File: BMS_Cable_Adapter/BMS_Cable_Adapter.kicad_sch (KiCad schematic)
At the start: 3 parts, among them J1 MicroFit_18Pin_Receptacle_Hea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, J2 MicroFit_10Pin_Receptacle_Hea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, J3 32Pin JAE

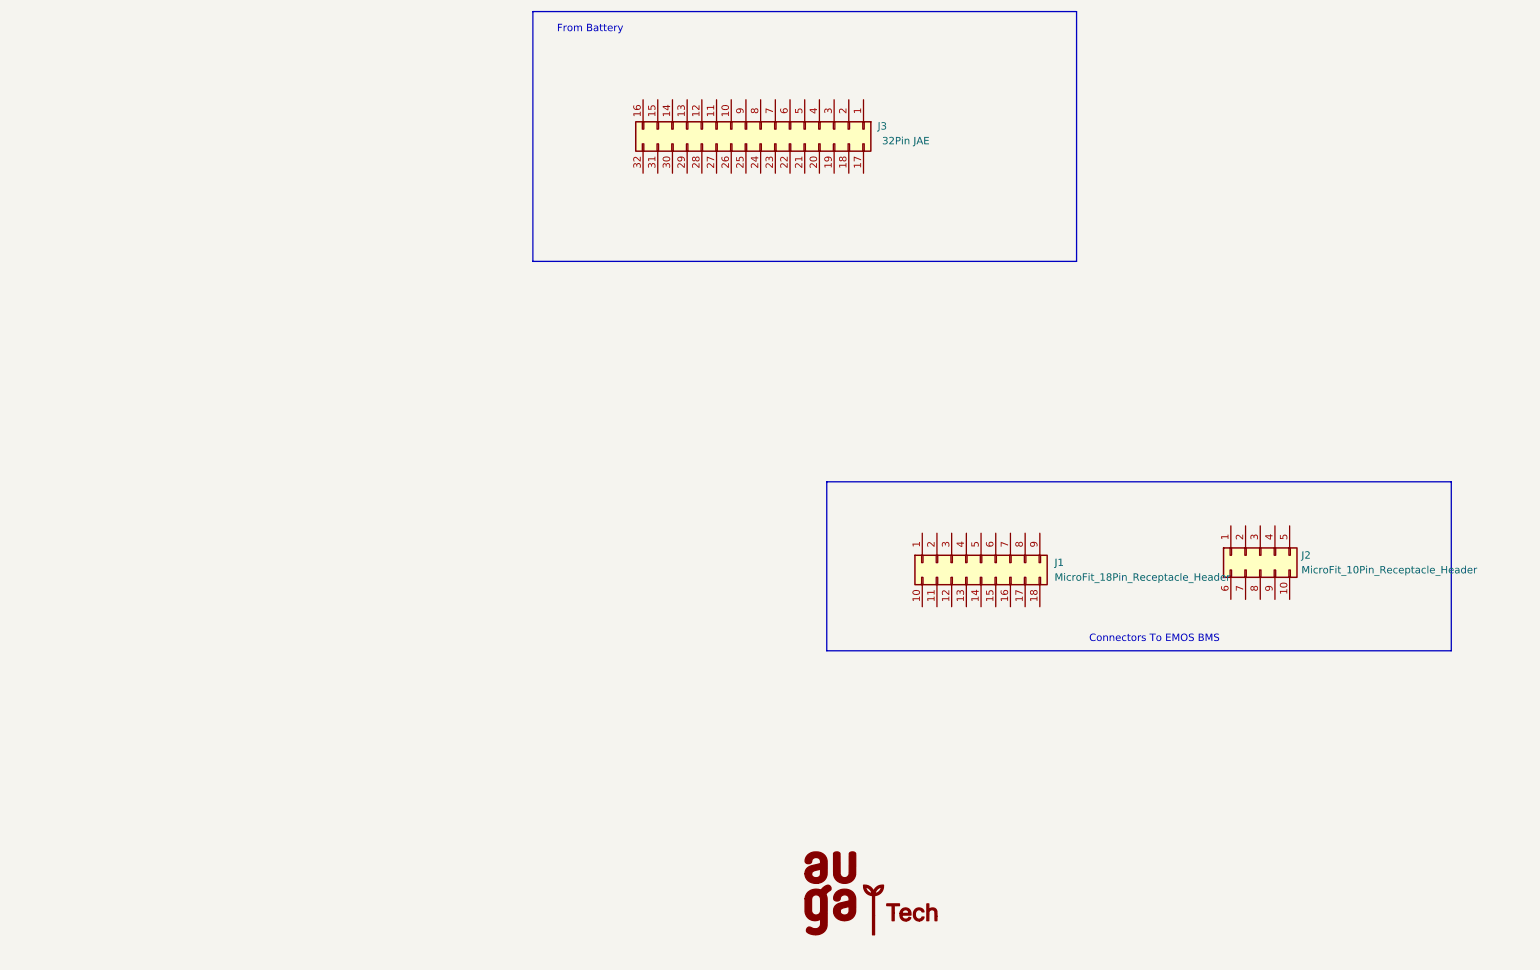
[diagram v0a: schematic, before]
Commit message: BMS Cable adapter done
Also libraries updated
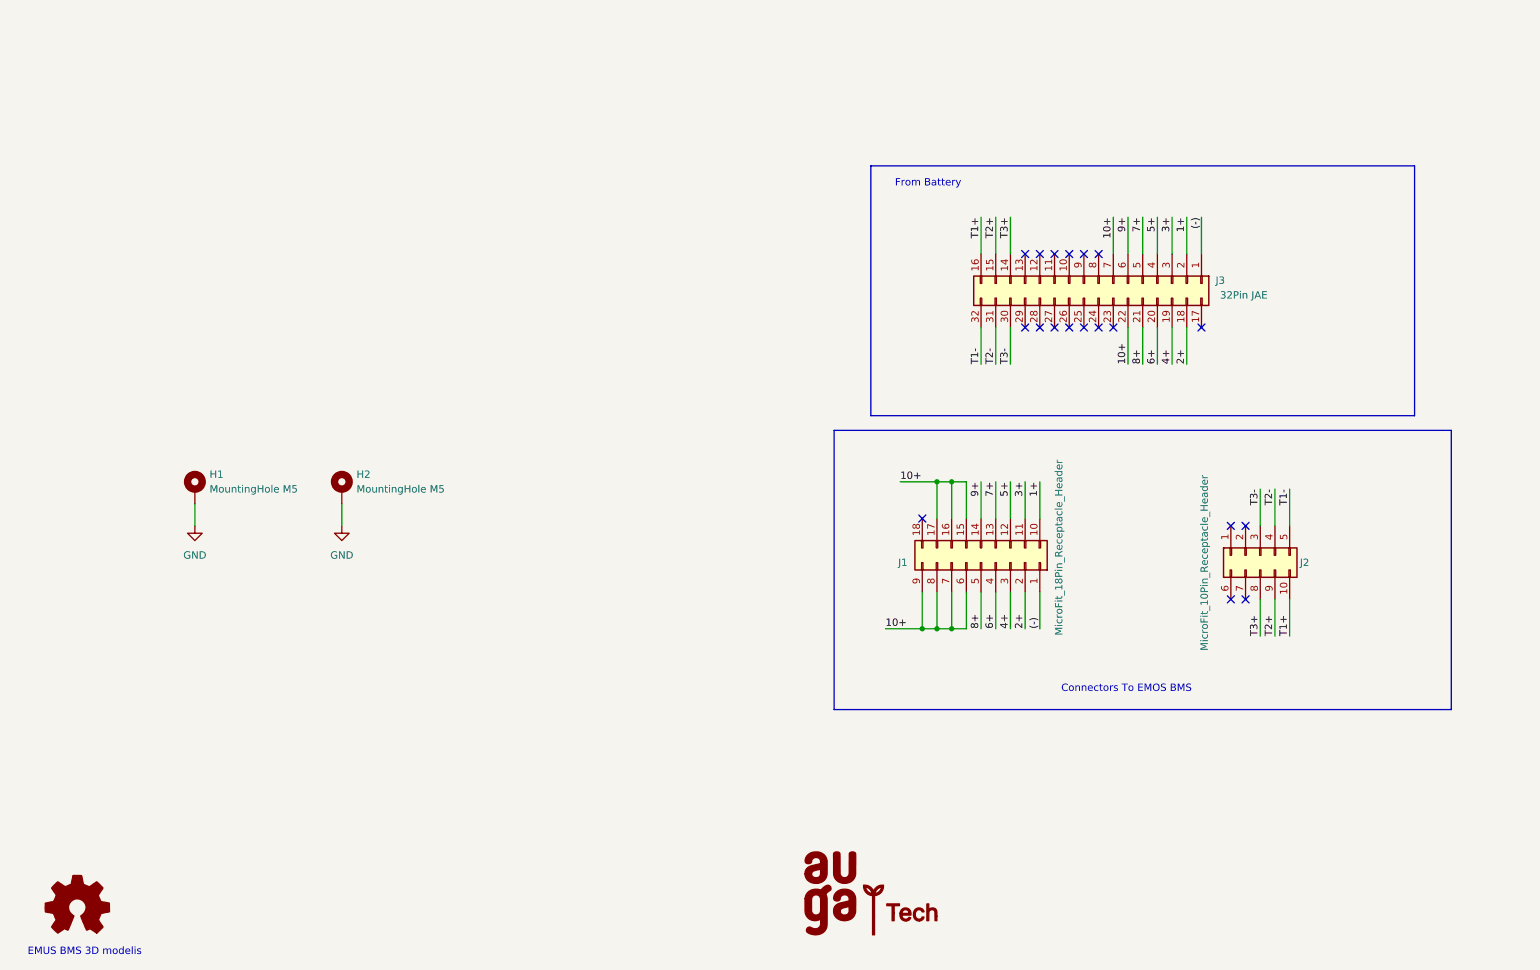
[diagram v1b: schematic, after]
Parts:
- added H1, H2: MountingHole M5, MountingHole:MountingHole_5.3mm_M5_Pad, symbol Mechanical:MountingHole_Pad
- added SYM1: Logo_Open_Hardware_Small, Calibration_Scale:Gauge_10mm_Type3_SilkScreenTop, symbol Graphic:Logo_Open_Hardware_Small
- J1: footprint Connector_Molex:Molex_Micro-Fit_3.0_43045-1800_2x09_P3.00mm_Horizontal -> 0_user_lib:Molex_Micro-Fit_BMI_Receptacle_18Pin_44764
- J2: footprint Connector_Molex:Molex_Micro-Fit_3.0_43045-1000_2x05_P3.00mm_Horizontal -> 0_user_lib:Molex_Micro-Fit_BMI_Receptacle_10Pin_44764
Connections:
- net (-): now reaches J1.1 (Pin_1)
- net (-): now also J3.1 (Pin_1)
- net 1+: now reaches J1.10 (Pin_10)
- net 1+: now also J3.2 (Pin_2)
- net 3+: now reaches J1.11 (Pin_11)
- net 3+: now also J3.3 (Pin_3)
- net 5+: now reaches J1.12 (Pin_12)
- net 5+: now also J3.4 (Pin_4)
- net 7+: now reaches J1.13 (Pin_13)
- net 7+: now also J3.5 (Pin_5)
- net 9+: now reaches J1.14 (Pin_14)
- net 9+: now also J3.6 (Pin_6)
- net 10+: now reaches J1.15 (Pin_15)
- net 10+: now also J1.16 (Pin_16), J1.17 (Pin_17), J1.6 (Pin_6), J1.7 (Pin_7), J1.8 (Pin_8), J1.9 (Pin_9), J3.22 (Pin_22), J3.7 (Pin_7)
- net 2+: now reaches J1.2 (Pin_2)
- net 2+: now also J3.18 (Pin_18)
- net 4+: now reaches J1.3 (Pin_3)
- net 4+: now also J3.19 (Pin_19)
- net 6+: now reaches J1.4 (Pin_4)
- net 6+: now also J3.20 (Pin_20)
- net 8+: now reaches J1.5 (Pin_5)
- net 8+: now also J3.21 (Pin_21)
- net T1+: now reaches J2.10 (Pin_10)
- net T1+: now also J3.16 (Pin_16)
- net T3-: now reaches J2.3 (Pin_3)
- net T3-: now also J3.30 (Pin_30)
- net T2-: now reaches J2.4 (Pin_4)
- net T2-: now also J3.31 (Pin_31)
- net T1-: now reaches J2.5 (Pin_5)
- net T1-: now also J3.32 (Pin_32)
- net T3+: now reaches J2.8 (Pin_8)
- net T3+: now also J3.14 (Pin_14)
- net T2+: now reaches J2.9 (Pin_9)
- net T2+: now also J3.15 (Pin_15)
- new net GND: H1.1, H2.1
- no-connect marks 0 -> 19
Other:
- note added: "EMUS BMS 3D modelis"
- company: (none) -> D. Vaitiekus
- title: (none) -> BMS to Cell Adapter
- moved on the sheet: J1, J3
